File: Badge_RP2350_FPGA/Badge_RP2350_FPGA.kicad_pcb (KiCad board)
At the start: 2 copper layers, 100 x 150 mm, 110 parts, among them J1 USB_C_Receptacle_USB2.0_16P, J2 Conn_01x03_Pin, J3 Conn_01x15_Pin, J4 Conn_01x15_Pin, SW1 SW_Push, SW12 On/Off, SW2 SW_Push, U1 RP2350_60QFN, U2 GW1N-LV9QN88C6_I5_, U3 ME6211C12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

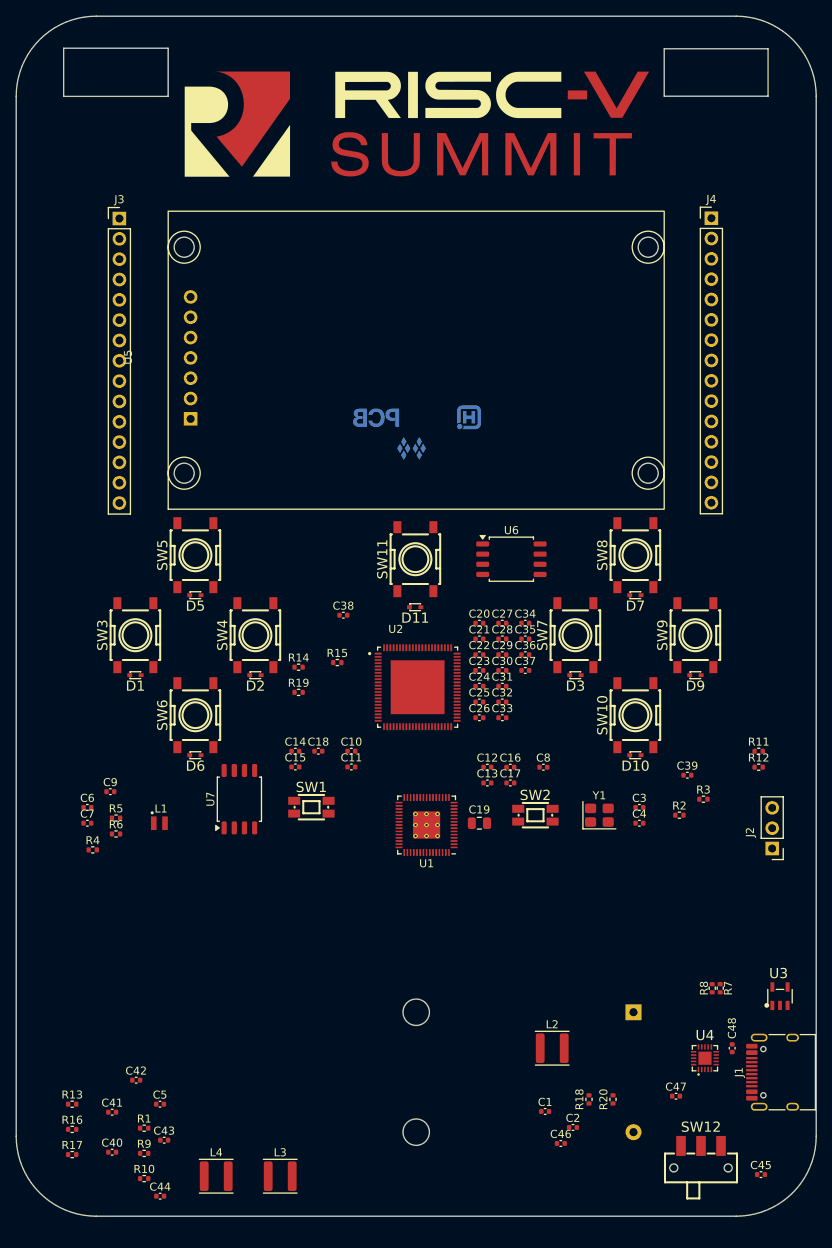
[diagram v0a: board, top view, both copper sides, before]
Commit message: M: pcb routing start, minor schematic changes
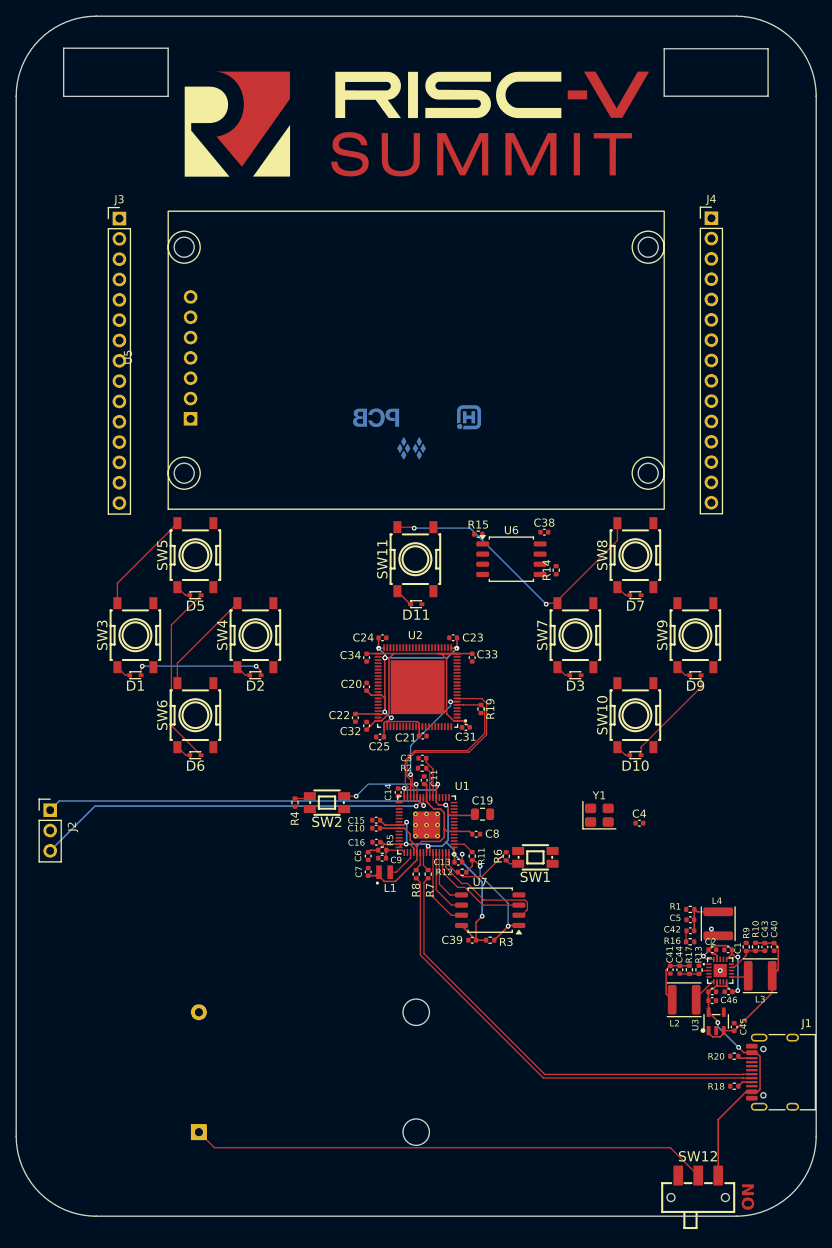
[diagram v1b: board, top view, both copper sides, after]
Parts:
- removed C12, C17, C18: 100n, Capacitor_SMD:C_0402_1005Metric
- removed C26, C27, C28, C29, C30: 100nF, Capacitor_SMD:C_0402_1005Metric
- removed C35, C36, C37: 10uF, Capacitor_SMD:C_0402_1005Metric
- moved J2 90.4 mm to (54.2, 149.2), turned to 0 degrees
- moved C40 86.6 mm to (144.8, 166.3), turned to -90 degrees
- moved R10 81.7 mm to (142.4, 166.3), turned to -90 degrees
- moved R16 80.7 mm to (134.2, 165.7), turned to 180 degrees
- moved R17 80.5 mm to (134.2, 169.2), turned to -90 degrees
- moved R13 80.1 mm to (135.3, 169.2), turned to -90 degrees
- moved R9 79.6 mm to (141.2, 166.3), turned to -90 degrees
- moved C43 78.9 mm to (143.6, 166.3), turned to -90 degrees
- moved R1 73.5 mm to (134.3, 161.6), turned to 180 degrees
- moved C41 72.0 mm to (131.8, 169.2), turned to -90 degrees
- moved C42 71.7 mm to (134.3, 164.3), turned to 180 degrees
- moved C44 70.9 mm to (132.9, 169.2), turned to -90 degrees
- moved L4 70.2 mm to (137.8, 163.4), turned to -90 degrees
- moved C5 70.2 mm to (134.3, 162.9), turned to 180 degrees
- moved L3 65.0 mm to (143.0, 169.9), turned to 180 degrees
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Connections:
- SW12 pad 1: +1v2 -> unconnected-(SW12-A-Pad1)
- SW12 pad 3: unconnected-(SW12-C-Pad3) -> +1v2
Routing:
- net +1v2: track 0.24 -> 86.3 mm, vias 0 -> 4
- net +3v3: track 0.00 -> 82.3 mm, vias 0 -> 8
- net Net-(BT1-+): track 0.00 -> 64.7 mm
- net USB_D-: track 0.00 -> 58.2 mm
- net USB_D+: track 0.00 -> 57.5 mm
- net /RP2350A/SWD: track 0.00 -> 49.4 mm, vias 0 -> 1
- net /RP2350A/SWCLK: track 0.00 -> 48.4 mm, vias 0 -> 1
- net VCC00_1_2_3V3: track 0.00 -> 47.3 mm, vias 0 -> 6
- net COL3: track 0.00 -> 37.1 mm, vias 0 -> 2
- net +1v1: track 0.00 -> 32.0 mm
- net TDO: track 0.00 -> 23.9 mm
- net ROW2: track 0.00 -> 23.1 mm
- net TCK: track 0.00 -> 22.9 mm
- net /RP2350A/FLASH_SS: track 0.00 -> 20.0 mm, vias 0 -> 2
- net ROW1: track 0.00 -> 16.8 mm, vias 0 -> 2
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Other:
- board text added: "ON"

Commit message: Routing progress
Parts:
- moved R14 27.1 mm to (90.4, 117.8), turned to -90 degrees
- moved R15 26.9 mm to (80.9, 114.5)
- moved U6 26.9 mm to (85.0, 117.6)
- moved C38 26.9 mm to (89.1, 114.3)
- moved C4 23.7 mm to (104.7, 146.0)
- moved Y1 19.3 mm to (104.6, 143.9), turned to 180 degrees
- moved R5 1.86 mm to (97.3, 155.3), turned to 180 degrees
- moved C16 1.66 mm to (96.3, 154.3)
- moved C23 0.96 mm to (105.6, 127.7), turned to 180 degrees
- moved SW12 0.40 mm to (135.2, 195.3)
- moved C9 0.25 mm to (95.5, 155.3)
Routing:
- net GPIO27_ADC1: track 0.00 -> 83.3 mm, vias 0 -> 1
- net L15A: track 0.00 -> 82.1 mm
- net GPIO28_ADC2: track 0.00 -> 82.1 mm, vias 0 -> 1
- net GPIO26_ADC0: track 0.00 -> 82.0 mm
- net GPIO29_ADC3: track 0.00 -> 81.1 mm, vias 0 -> 1
- net L22A: track 0.00 -> 78.8 mm
- net L22B: track 0.00 -> 75.4 mm
- net B13A: track 0.00 -> 64.2 mm, vias 0 -> 1
- net B13B: track 0.00 -> 61.6 mm, vias 0 -> 1
- net B17A: track 0.00 -> 59.5 mm, vias 0 -> 1
- net B11A: track 0.00 -> 57.6 mm
- net B11B: track 0.00 -> 57.4 mm, vias 0 -> 1
- net B17B: track 0.00 -> 57.3 mm, vias 0 -> 1
- net MODE0: track 0.00 -> 52.0 mm, vias 0 -> 1
- net MODE1: track 0.00 -> 51.0 mm, vias 0 -> 1
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
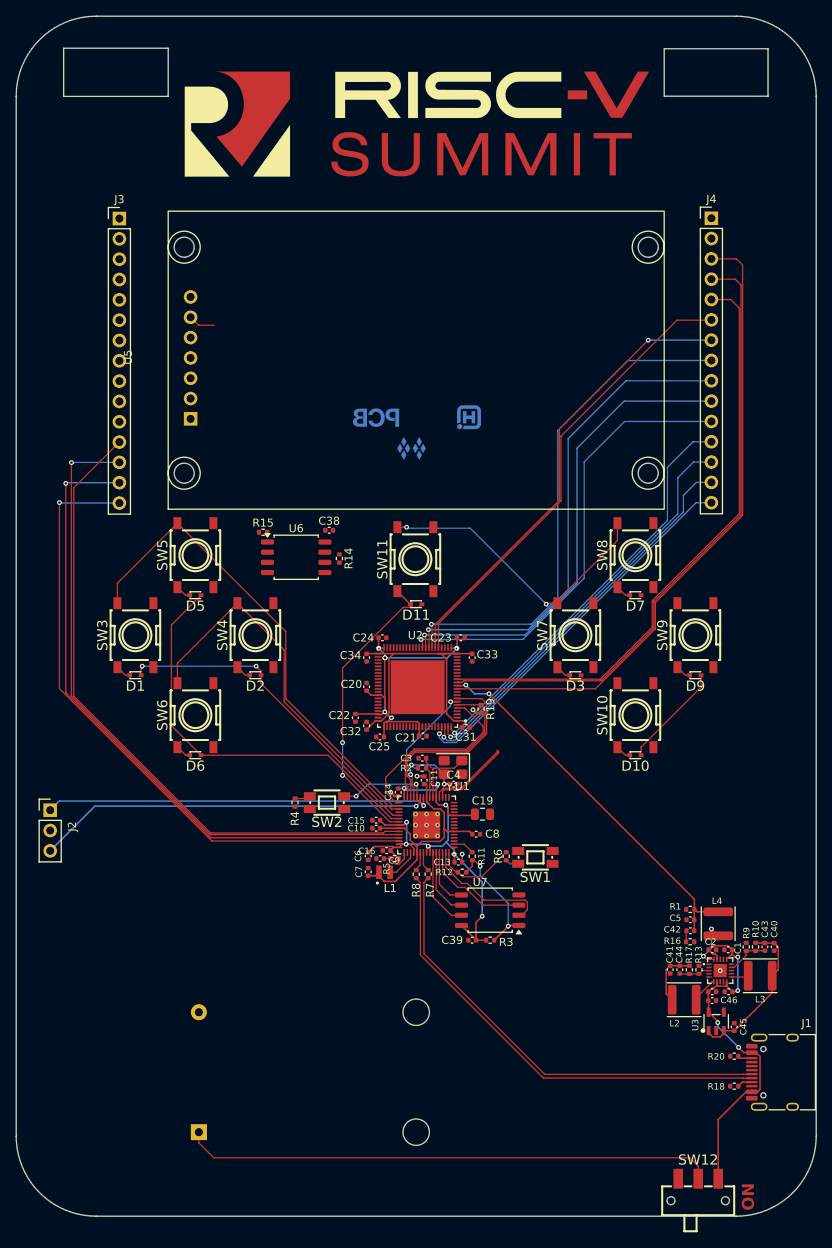
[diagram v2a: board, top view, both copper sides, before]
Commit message: Update PCB routing
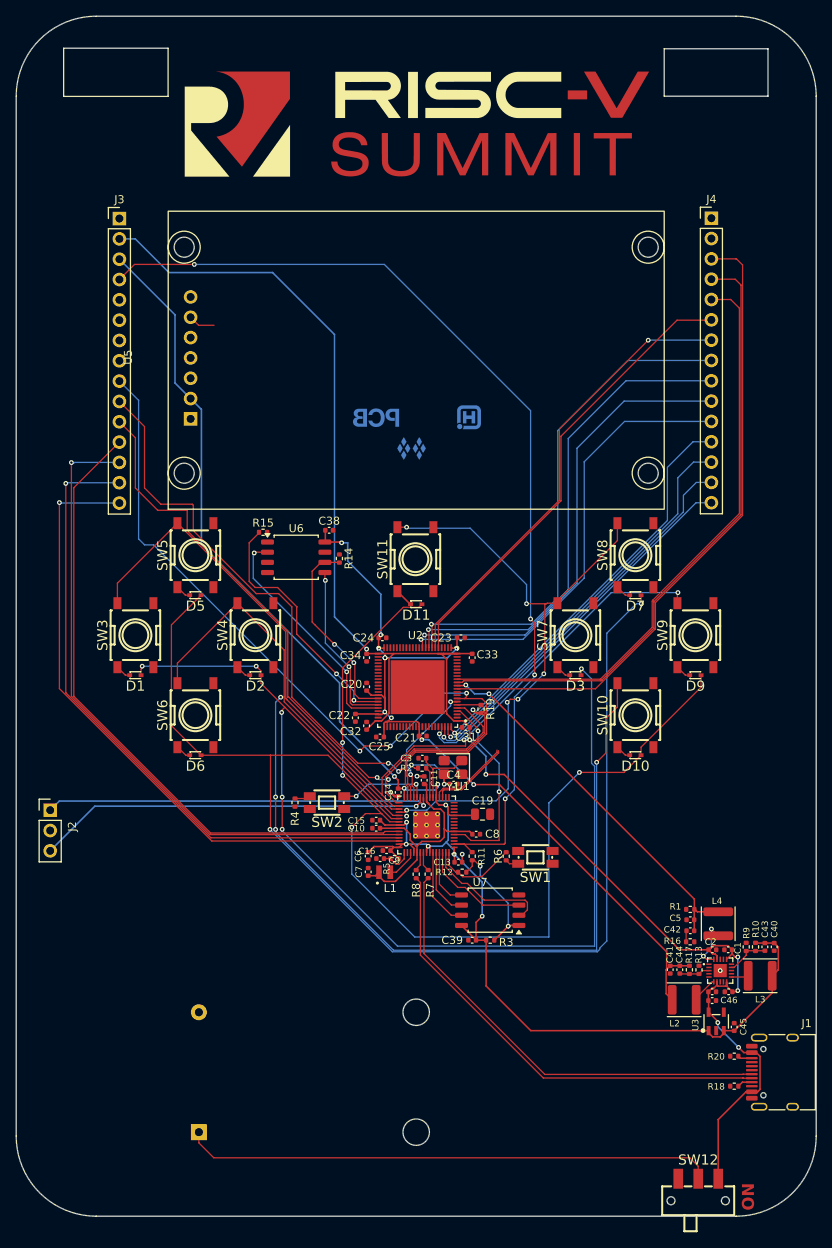
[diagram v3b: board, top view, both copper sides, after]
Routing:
- net GPIO0: track 2.67 -> 124.7 mm, vias 0 -> 4
- net +1v2: track 86.3 -> 203.3 mm, vias 4 -> 7
- net +3v3: track 83.7 -> 200.1 mm, vias 8 -> 9
- net ROW2: track 51.1 -> 154.9 mm, vias 0 -> 2
- net COL2: track 47.8 -> 146.0 mm, vias 0 -> 4
- net ROW1: track 41.9 -> 138.8 mm, vias 2 -> 6
- net TDO: track 23.9 -> 100.4 mm, vias 0 -> 3
- net ROW3: track 49.2 -> 118.1 mm, vias 2 -> 4
- net TCK: track 22.9 -> 90.9 mm, vias 0 -> 2
- net VCC00_1_2_3V3: track 47.3 -> 109.9 mm, vias 6 -> 10
- net TMS: track 23.5 -> 86.1 mm, vias 0 -> 2
- net COL1: track 60.4 -> 111.3 mm, vias 0 -> 2
- net COL3: track 37.1 -> 79.0 mm, vias 2 -> 6
- net /GW1NR 9K FPGA/MCS_N: track 0.00 -> 31.7 mm, vias 0 -> 2
- net /GW1NR 9K FPGA/MISO_SD1: track 0.00 -> 29.6 mm, vias 0 -> 2
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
